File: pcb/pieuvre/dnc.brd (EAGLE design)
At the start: 97.2 x 88 mm, 143 parts, among them IC1 LM2596S, IC2 74ACT244SC, Q1 IRF9321PBF, Q10 FDN337N, Q11 FDN337N, Q12 BSS138, Q13 BSS138, Q14 FDN337N, Q2 BSS670, Q3 BSS138, Q4 BSS670, Q5 BSS138, Q6 BSS316, Q7 BSS138, Q8 BSS138, Q9 BSS670, U1 MAX202CDWR, U2 74HCT595D, U3 TC7SU04F, U4 AL8805WS, U5 AL8805WS, U6 TC7SU04F, X1 USB

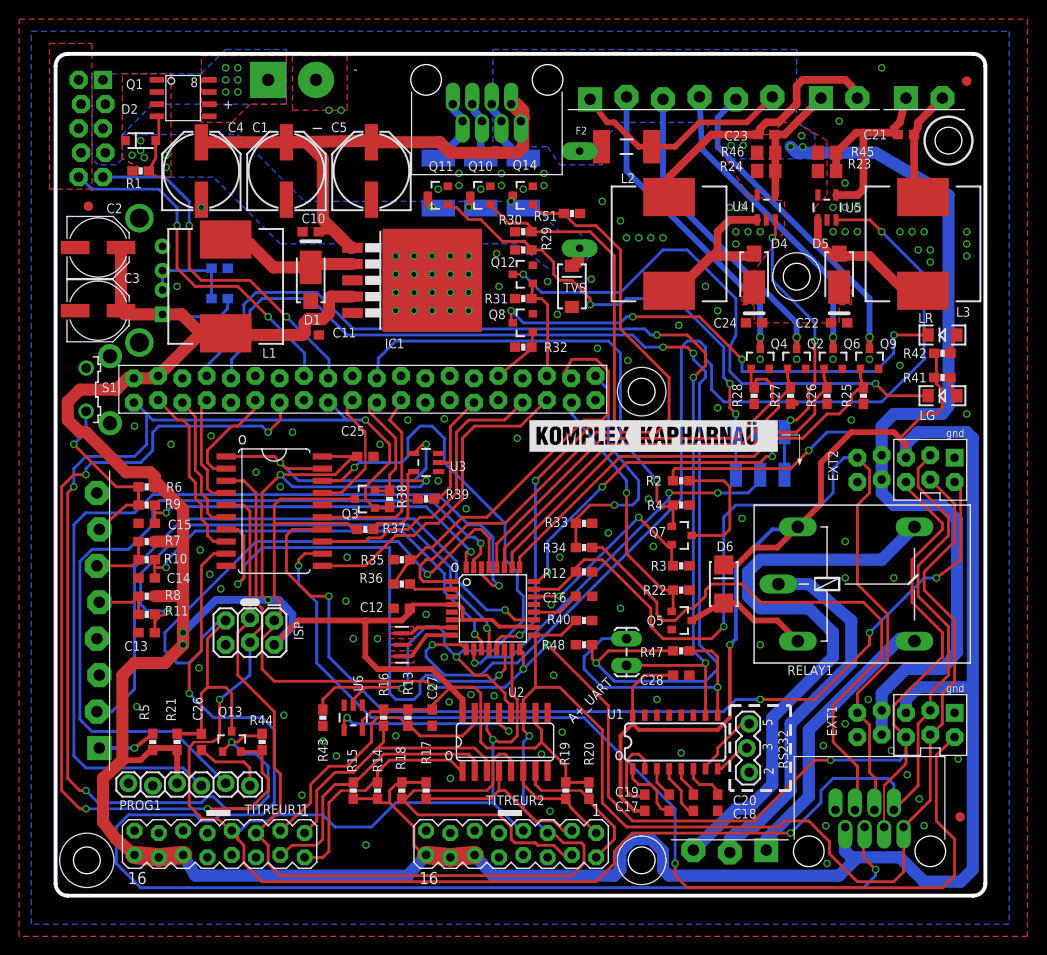
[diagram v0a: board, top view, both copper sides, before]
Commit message: major changes : - carte pieuvre - carte relais - correctif v1 : usb + pin A7 ! - enclosure
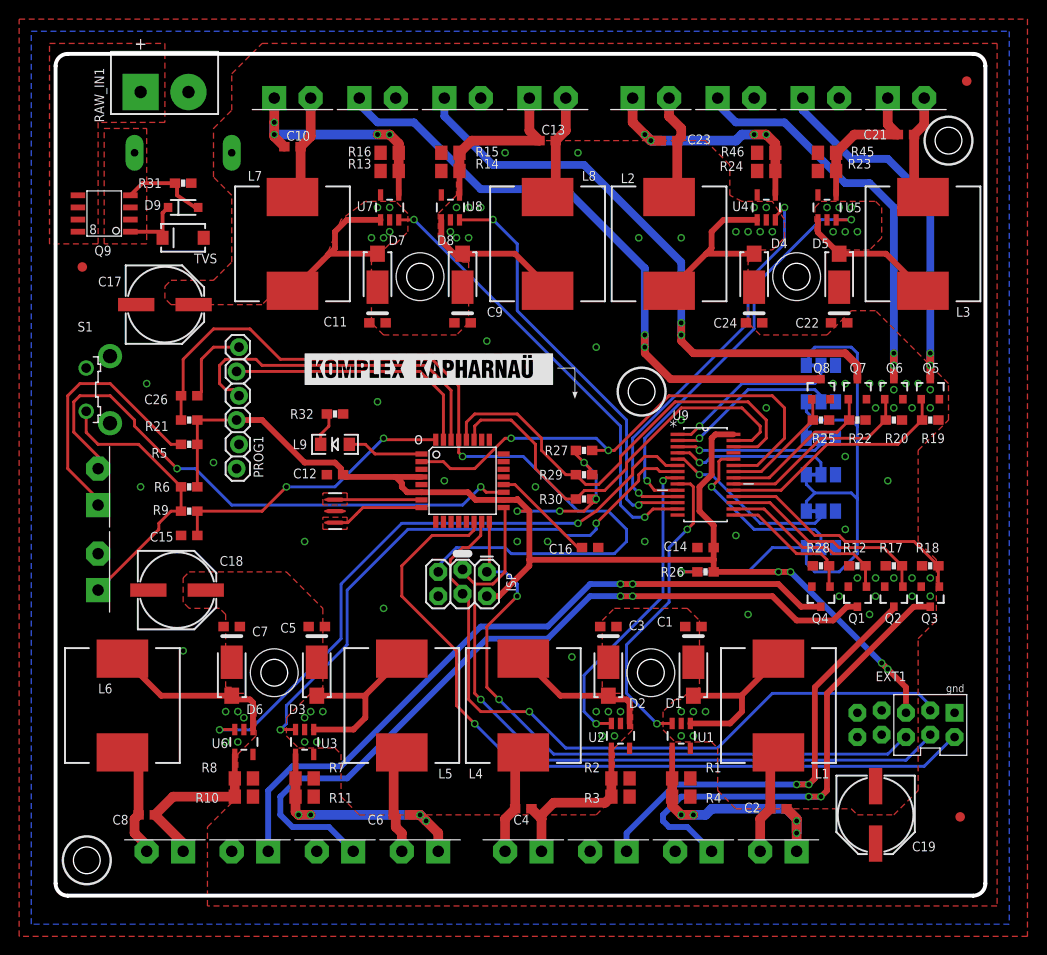
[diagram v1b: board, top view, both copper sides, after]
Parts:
- removed A+_UART: (no value), SparkFun:1X02_LOCK_LONGPADS
- removed C20, C25, C27, C28: 0.1uF, rcl:C0603
- removed EXT2: EXT, pierre_vv:EXTPINDNC
- removed F2, F3, F4, F5: PTC1812, pierre_vv:PTC_1812
- removed GYRO-LED: PLUG-6, pierre_vv:PLUG_06
- removed IC1: LM2596S, national-semiconductor:TO263-5
- removed IC2: 74ACT244SC, 74xx-us:SO20W
- removed INPUT: PLUG-8, pierre_vv:PLUG_08
- removed JP1: CHARGEUR, pierre_vv:2X5_LOCK
- removed LG, LR: (no value), SparkFun-LED:LED-1206
- removed Q10, Q11, Q14: FDN337N, SparkFun-DiscreteSemi:SOT23-3
- removed Q12, Q13: BSS138, SparkFun-DiscreteSemi:SOT23-3
- removed R33, R35, R48: 20K, SparkFun-Passives:0603-RES
- removed R34, R36, R37, R38, R39, R40, R43, R44, R47: 10K, SparkFun-Passives:0603-RES
- removed R41, R42: 1K, SparkFun-Passives:0603-RES
- removed R49: 22K, SparkFun-Passives:0603-RES
- removed R50: 33K, SparkFun-Passives:0603-RES
- removed R51: 100K, SparkFun-Passives:0603-RES
- removed RAW_IN: DNC_IN2PWR, pierre_vv:DNC_IN2_PWR
- removed RELAY: PLUG-3, pierre_vv:PLUG_03
- removed RELAY1: G5L, relay:G5LE
- removed RGB-LED: RJ45-RGBLED, con-amphenol-rj45-ld:RJ45-TRAFO
- removed RS232: (no value), SparkFun-Connectors:1X03_LOCK
- removed TITREUR1, TITREUR2: DNC_TITREUR, pierre_vv:DNC_TITREUR
- removed U$8: RJ45-EXTDNC, con-amphenol-rj45-ld:RJ45-TRAFO
- removed X1: USB, pierre_vv:USB_F_SATISTRONIC
- added C6, C8: 1uF, rcl:C0603
- added C7, C9: 0.1uF, rcl:C0603
- added D3, D7, D8: 40v5A, pierre_vv:DO-221
- added D9: 10V, SparkFun-DiscreteSemi:SOD-123
- added FAN1, FAN2, FAN3, FAN4, FAN5, FAN6, FAN7, FAN8, LED10W3, LED10W4, LED10W5, LED10W6, LED10W7, LED10W8, POT, SWITCH: PLUG-2, pierre_vv:PLUG_02
- added L4, L5, L6, L7, L8: 100nH2.4A, SparkFun:CDRH125
- added L9: LG, SparkFun-LED:LED-1206
- added RAW_IN1: DNC_IN2PWR, pierre_vv:DNC_IN2_PWR
- added SJ3, SJ4, SJ5, SJ6: JUMPER-PAD-3-2OF3_NC_BY_TRACE_LARGE, SparkFun-Passives:PAD-JUMPER-3-2OF3_NC_BY_TRACE_YES_SILK_LARGE
- added U$3, U$5: RADIATEUR, pierre_vv:RADIATEUR_577102B00000G
- added U7, U8: AL8805WS, SparkFun-PowerIC:SOT23-5
- added U9: PCA9685PW, pierre_vv:SOP65P640X110-28N
- C1, C5: value 220uF -> 0.1uF; device SparkFun:PANASONIC_E -> rcl:C0603
- C10: value 0.1uF -> 1uF
- C14: value 1uF -> 0.1uF
- C17, C18, C19: value 0.1uF -> 220uF; device rcl:C0603 -> SparkFun:PANASONIC_E
- C2: value 100u -> 1uF; device rcl:PANASONIC_D -> rcl:C0603
- C3: value 100u -> 0.1uF; device rcl:PANASONIC_D -> rcl:C0603
- C4: value 220uF -> 1uF; device SparkFun:PANASONIC_E -> rcl:C0603
- D2: value 10V -> 40v5A; device SparkFun-DiscreteSemi:SOD-123 -> pierre_vv:DO-221
- D6: value (none) -> 40v5A; device SparkFun-DiscreteSemi:SMA-DIODE_ALT -> pierre_vv:DO-221
- L1: value 68nH3A -> 100nH2.4A
- Q1: value IRF9321PBF -> BSS316; device pierre_vv:SO-8 -> SparkFun-DiscreteSemi:SOT23-3
- Q2, Q4: value BSS670 -> BSS316
- Q3, Q5, Q7, Q8: value BSS138 -> BSS316
- Q9: value BSS670 -> IRF9321PBF; device SparkFun-DiscreteSemi:SOT23-3 -> pierre_vv:SO-8
- R1, R13, R14: value 100K -> 0.110; device SparkFun-Passives:0603-RES -> rcl:R0805
- R10, R11: value 33K -> OPT; device SparkFun-Passives:0603-RES -> rcl:R0805
- R12: value 5.1K -> 100K
- R15, R16, R4: value 100K -> OPT; device SparkFun-Passives:0603-RES -> rcl:R0805
- R2: value 100k1% -> 0.110; device SparkFun-Passives:0603-RES -> rcl:R0805
- R26, R32: value 100K -> 1K
- R27, R29, R30: value 100K -> 10K
- R3: value 10k1% -> OPT; device SparkFun-Passives:0603-RES -> rcl:R0805
- R7, R8: value 56K -> 0.110; device SparkFun-Passives:0603-RES -> rcl:R0805
- SJ1, SJ2: value JUMPER-PAD-3-NO -> JUMPER-PAD-3-2OF3_NC_BY_TRACE_LARGE; device SparkFun-Passives:PAD-JUMPER-3-NO_YES_SILK_FULL_BOX_WIDE_SPACING -> SparkFun-Passives:PAD-JUMPER-3-2OF3_NC_BY_TRACE_YES_SILK_LARGE
- U$4: value RASPIA+ -> RADIATEUR; device pierre_vv:RASPIA+ -> pierre_vv:RADIATEUR_577102B00000G
- U1: value MAX202CDWR -> AL8805WS; device SparkFun-DigitalIC:SO016 -> SparkFun-PowerIC:SOT23-5
- U2: value 74HCT595D -> AL8805WS; device IC:SO16 -> SparkFun-PowerIC:SOT23-5
- U3, U6: value TC7SU04F -> AL8805WS; device SparkFun-DigitalIC:SOT23-5 -> SparkFun-PowerIC:SOT23-5
- moved LED10W1 111.8 mm to (11.4, 0.64), turned to 180 degrees
- moved C2 92.2 mm to (75.6, 5.08), turned to 180 degrees
- moved LED10W2 90.1 mm to (38.1, 0.64), turned to 180 degrees
- moved Q1 87.6 mm to (83.8, 27.3), turned to 180 degrees
- moved R1 85.0 mm to (65.4, 8.26), turned to 0 degrees
- moved Q9 81.4 mm to (5.08, 67.3), turned to 180 degrees
- moved C4 74.7 mm to (48.9, 5.08), turned to 180 degrees
- moved D2 74.3 mm to (57.8, 19.1), turned to 90 degrees
- moved C17 74.1 mm to (11.4, 57.8), turned to 0 degrees
- moved L1 72.5 mm to (75.6, 15.9)
- moved U$4 69.8 mm to (38.1, 60.7), flipped to the bottom
- moved R15 67.4 mm to (41.3, 73.7), turned to 180 degrees
- moved C13 66.3 mm to (51.4, 74.9), turned to 0 degrees
- moved R14 65.2 mm to (41.3, 71.8), turned to 180 degrees
- moved C1 63.9 mm to (66.7, 24.1), turned to 0 degrees
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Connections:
- removed net +3V3: Q13.1, Q3.1, R38.2, R44.2, U$4.1, U$4.17
- removed net /REG_RCK_5V=ACTIVE_CS: U2.13, U6.4
- removed net ALL_CS_ENABLE_ACTIVE_LOW_5V: IC2.1, IC2.19, U3.4
- removed net ANALOG_RAW: AT328.22, Q7.2, R3.2
- removed net ATMEGA_CS: IC2.13, U$4.33
- removed net ATMEGA_CS_5V: AT328.14, IC2.7
- removed net CHARGING: JP1.2, U$4.16
- removed net CS_TRIGGER_ACTIVE_HIGH: R39.2, U$4.29, U3.2
- removed net DIGITAL_LED2_OR_FLEX3: AT328.24, SJ1.2
- removed net EXT1_CS: IC2.8, U$4.3
- removed net EXT2_CS: IC2.6, U$4.5
- removed net EXT2_CS_5V: EXT2./CS, IC2.14
- removed net EXT3_CS: IC2.4, U$4.7
- removed net EXT3_CS_5V: IC2.16
- removed net GYRO_1: AT328.28, Q4.1, R28.2
- removed net GYRO_2: AT328.27, Q2.1, R27.2
- removed net GYRO_3: AT328.26, Q6.1, R26.2
- removed net GYRO_4: AT328.25, Q9.1, R25.2
- removed net INT_ATMEGA: R35.2, R36.1, U$4.38
- removed net INT_ATMEGA_5V: AT328.2, R36.2
- removed net INT_TELECO: R33.2, R34.1, U$4.40
- removed net INT_TELECO_5V: R34.2, U$8.4
- removed net LEDR: LR.C, Q8.3
- removed net LED_G: Q12.1, R31.2, U$4.36
- removed net LED_R: Q8.1, R32.2, U$4.32
- removed net LG: LG.C, Q12.3
- removed net MISO: Q3.2, R38.1, U$4.21
- removed net MOSI: IC2.17, U$4.19
- removed net N$1: D1.C, IC1.2, L1.1
- removed net N$19: F3.1, Q10.3
- removed net N$20: INPUT.6, R10.1, R7.1
- removed net N$21: LR.A, R42.1
- removed net N$23: INPUT.5, R11.1, R8.1
- removed net N$24: C19.2, U1.2
- removed net N$26: R49.2, R50.2, X1.DM, X1.DP
- removed net N$29: F5.2, RGB-LED.3, RGB-LED.4
- removed net N$50: C18.2, U1.5
- removed net N$51: C18.1, U1.4
- removed net N$52: C17.2, U1.3
- removed net N$53: C17.1, U1.1
- removed net PRXD_PIN2_RS232: RS232.1, U1.7
- removed net PTXD_PIN3_RS232: RS232.2, U1.8
- removed net PUSH2: AT328.11, C14.1, R10.2
- removed net PUSH3: AT328.12, C13.1, R11.2
- removed net PWM_FLEX_1: AT328.1, Q14.1, R51.2
- removed net PWM_FLEX_2: AT328.13, Q10.1, R30.2
- removed net PWM_FLEX_3: Q11.1, R29.2, SJ1.3, SJ2.3
- removed net PWM_LED2_OR_FLEX3: AT328.10, SJ2.2
- removed net RAW_POL_PROTECTED: D2.C, F1.P$1MOV, Q1.1, Q1.2, Q1.3, TVS.C
- removed net RAW_UNPROTECTED: JP1.3, JP1.5, JP1.7, JP1.9, Q1.5, Q1.6, Q1.7, Q1.8, RAW_IN.1
- removed net READ_BATTERY: Q7.1, R4.2, U$4.22
- removed net REG_RCK: IC2.2, U$4.11
- removed net REG_RCK_5V: IC2.18, R43.2, U2.12, U6.2
- removed net RELAY1: Q5.1, R22.2, U$4.37
- removed net RELAY_CHARGE_BOARD: JP1.1, U$4.18
- removed net RESET: Q13.2, R44.1, U$4.13
- removed net RST1: R16.1, TITREUR1.1, U2.3
- removed net RST2: R14.1, TITREUR1.2, U2.1
- removed net RST3: R13.1, TITREUR1.3, U2.15
- removed net RST4: R15.1, TITREUR1.4, U2.2
- removed net RST5: R19.1, TITREUR2.1, U2.6
- removed net RST6: R20.1, TITREUR2.2, U2.7
- removed net RST7: R17.1, TITREUR2.3, U2.4
- removed net RST8: R18.1, TITREUR2.4, U2.5
- removed net RXA+: R47.1, R48.2, U$4.10
- removed net RXA+_5V: A+_UART.2, R47.2, U1.9
- removed net SCK: IC2.15, U$4.23
- removed net TELECO_CS: IC2.11, U$4.35
- removed net TELECO_CS_5V: IC2.9, U$8.3
- removed net TXA+_5V: A+_UART.1, U$4.8, U1.10
- new net A0: SJ1.2, U9.1
- new net A1: SJ2.2, U9.2
- new net A2: SJ3.2, U9.3
- new net A3: SJ4.2, U9.4
- new net A4: SJ5.2, U9.5
- new net A5: SJ6.2, U9.24
- new net LED: AT328.1, L9.A
- new net LED+3: C4.1, LED10W3.1, R2.1, R3.1, U2.4
- new net LED+4: C2.1, LED10W4.1, R1.1, R4.1, U1.4
- new net LED+5: C21.1, LED10W5.1, R23.1, R45.1, U5.4
- new net LED+6: C23.1, LED10W6.1, R24.1, R46.1, U4.4
- new net LED+7: C13.1, LED10W7.1, R14.1, R15.1, U8.4
- new net LED+8: C10.1, LED10W8.1, R13.1, R16.1, U7.4
- new net LED-3: C4.2, L4.2, LED10W3.2
- new net LED-4: C2.2, L1.2, LED10W4.2
- new net LED-5: C21.2, L3.2, LED10W5.2
- new net LED-6: C23.2, L2.2, LED10W6.2
- new net LED-7: C13.2, L8.2, LED10W7.2
- new net LED-8: C10.2, L7.2, LED10W8.2
- new net OE: AT328.2, R27.1, U9.23
- new net PWM_FAN1: Q4.1, R28.2, U9.15
- new net PWM_FAN2: Q1.1, R12.2, U9.16
- new net PWM_FAN3: Q2.1, R17.2, U9.17
- new net PWM_FAN4: Q3.1, R18.2, U9.18
- new net PWM_FAN5: Q5.1, R19.2, U9.19
- new net PWM_FAN6: Q6.1, R20.2, U9.20
- new net PWM_FAN7: Q7.1, R22.2, U9.21
- new net PWM_FAN8: Q8.1, R25.2, U9.22
- new net PWM_LED_3: U2.3, U9.8
- new net PWM_LED_4: U1.3, U9.9
- new net PWM_LED_5: U5.3, U9.10
- new net PWM_LED_6: U4.3, U9.11
- new net PWM_LED_7: U8.3, U9.12
- new net PWM_LED_8: U7.3, U9.13
- new net RAW_POL_PROTECTED1: D9.C, F1.P$1MOV, Q9.1, Q9.2, Q9.3, TVS.C
- new net RAW_UNPROTECTED1: Q9.5, Q9.6, Q9.7, Q9.8, RAW_IN1.1
- new net SCL: AT328.28, R29.1, U9.26
- new net SDA: AT328.27, R30.1, U9.27
- net +5V: now also C14.1, R26.2, R27.2, R29.2, R30.2, U9.28; no longer C11.1, C19.1, C2.+, C25.1, C27.1, C28.1, C3.+, D6.C, EXT2.5V, IC1.4, IC2.20, L1.2, R13.2, R14.2, R15.2, R16.2, R17.2, R18.2, R19.2, R20.2, R37.2, R41.2, R42.2, R50.1, R7.2, R8.2, RELAY1.2, TITREUR1.12, TITREUR1.14, TITREUR1.16, TITREUR2.12, TITREUR2.14, TITREUR2.16, U$4.2, U$4.4, U$8.1, U1.16, U2.10, U2.16, U3.5, U6.5, X1.+
- net CODE: no longer AT328.23, EXT2.RETOURANALOG, R12.1, U$8.6
- net EXT1_CS_5V: now also AT328.14; no longer IC2.12
- net FLOAT1: now also POT.2; no longer INPUT.2
- net GND: now also C1.2, C17.-, C18.-, C19.-, C3.2, C5.2, C7.2, C9.2, Q1.2, Q3.2, Q7.2, R12.1, R17.1, R18.1, R19.1, R20.1, R31.2, R32.2, RAW_IN1.2, SJ1.1, SJ2.1, SJ3.1, SJ4.1, SJ5.1, SJ6.1, SWITCH.2, U1.2, U2.2, U3.2, U6.2, U7.2, U8.2, U9.14, U9.25; no longer C1.-, C10.2, C13.2, C2.-, C20.2, C25.2, C27.2, C28.2, C3.-, C4.-, C5.-, D1.A, EXT2.1_GND, EXT2.GND2, IC1.3, IC1.5, IC1.THERMAL, IC2.10, INPUT.4, INPUT.8, JP1.10, JP1.4, JP1.6, JP1.8, Q10.2, Q11.2, Q12.2, Q14.2, Q9.2, R1.2, R12.2, R26.1, R27.1, R29.1, R3.1, R30.1, R31.1, R32.1, R33.1, R35.1, R39.1, R4.1, R40.1, R43.1, R48.1, R49.1, R51.1, RAW_IN.2, RS232.3, TITREUR1.11, TITREUR1.13, TITREUR1.15, TITREUR1.8, TITREUR2.11, TITREUR2.13, TITREUR2.15, TITREUR2.8, U$4.14, U$4.20, U$4.25, U$4.30, U$4.34, U$4.39, U$4.6, U$4.9, U$8.2, U1.15, U2.8, U3.3, U6.3, X1.-, X1.S1, X1.S2
- net LED+1: now also C6.1, R11.1, R7.1, U3.4; no longer C23.1, R24.1, R46.1, U4.4
- net LED+2: now also C8.1, R10.1, R8.1, U6.4; no longer C21.1, R23.1, R45.1, U5.4
- net LED-1: now also C6.2, L5.2; no longer C23.2, L2.2
- net LED-2: now also C8.2, L6.2; no longer C21.2, L3.2
- net MISO_5V: no longer EXT2.MISO, Q3.3, R37.1, U$8.5
- net MOSI_5V: no longer EXT2.MOSI, IC2.3, TITREUR1.7, TITREUR2.7, U$8.8, U2.14
- net N$10: now also D7.A, L7.1, U7.1; no longer GYRO-LED.2, Q4.3
- net N$11: now also D8.A, L8.1, U8.1; no longer GYRO-LED.3, Q2.3
- net N$12: now also FAN2.1, Q1.3; no longer GYRO-LED.4, Q6.3
- net N$13: now also FAN3.1, Q2.3; no longer GYRO-LED.5, Q9.3
- net N$14: now also FAN4.1, Q3.3; no longer F4.2, RGB-LED.7, RGB-LED.8
- net N$15: now also FAN5.1, Q5.3; no longer RELAY.3, RELAY1.O
- net N$16: now also FAN6.1, Q6.3; no longer D6.A, Q5.3, RELAY1.1
- net N$17: now also FAN7.1, Q7.3; no longer F4.1, Q11.3
- net N$18: now also FAN8.1, Q8.3; no longer LG.A, R41.1
- net N$22: now also SWITCH.1; no longer INPUT.7
- net N$25: now also POT.1; no longer INPUT.1
- net N$3: now also D1.A, L1.1, U1.1; no longer Q7.3, R2.1
- net N$30: now also R26.1, SJ1.3, SJ2.3, SJ3.3, SJ4.3, SJ5.3, SJ6.3; no longer F5.1, Q14.3
- net N$35: now also L9.C, R32.1; no longer C20.1, U1.6
- net N$4: now also FAN1.1, Q4.3; no longer RELAY.1, RELAY1.S
- net N$5: now also D2.A, L4.1, U2.1; no longer F2.2, GYRO-LED.1, GYRO-LED.6
- net N$8: now also D3.A, L5.1, U3.1; no longer RELAY.2, RELAY1.P
- net N$9: now also D6.A, L6.1, U6.1; no longer F3.2, RGB-LED.5, RGB-LED.6
- net PROTECT_GATE: now also D9.A, Q9.4, R31.1; no longer D2.A, Q1.4, R1.1
- net PWM_LED_1: now also U6.3, U9.6; no longer AT328.9, U5.3
- net PWM_LED_2: now also U3.3, U9.7; no longer SJ1.1, SJ2.1, U4.3
- net RAW_FUSED: now also C1.1, C11.1, C17.+, C18.+, C19.+, C3.1, C5.1, C7.1, C9.1, D1.C, D2.C, D3.C, D6.C, D7.C, D8.C, FAN1.2, FAN2.2, FAN3.2, FAN4.2, FAN5.2, FAN6.2, FAN7.2, FAN8.2, R1.2, R10.2, R11.2, R13.2, R14.2, R15.2, R16.2, R3.2, R4.2, R7.2, R8.2, U1.5, U2.5, U3.5, U6.5, U7.5, U8.5; no longer C1.+, C10.1, C4.+, C5.+, EXT1.RAW, EXT1.RAW2, EXT2.RAW, EXT2.RAW2, F2.1, IC1.1, RGB-LED.1, RGB-LED.2
- net RESET_5V: no longer Q13.3
- net SCK_5V: no longer EXT2.SCK, IC2.5, R40.2, TITREUR1.5, TITREUR2.5, U$8.7, U2.11
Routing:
- net +5V: track 579.0 -> 145.5 mm, vias 6 -> 8
- net RAW_FUSED: track 180.6 -> 0.00 mm, vias 6 -> 0
- net MOSI_5V: track 227.8 -> 74.8 mm, vias 3 -> 1
- net TELECO_CS_5V: track 143.6 -> 0.00 mm, vias 2 -> 0
- net SCK_5V: track 211.8 -> 75.7 mm
- net +3V3: track 123.3 -> 0.00 mm, vias 4 -> 0
- net RXA+: track 116.4 -> 0.00 mm, vias 3 -> 0
- net TXA+_5V: track 108.2 -> 0.00 mm, vias 3 -> 0
- net EXT2_CS_5V: track 103.6 -> 0.00 mm, vias 4 -> 0
- net MISO_5V: track 169.7 -> 68.6 mm, vias 4 -> 2
- net CODE: track 97.4 -> 0.00 mm, vias 1 -> 0
- net RESET: track 91.3 -> 0.00 mm, vias 4 -> 0
- net REG_RCK_5V: track 81.7 -> 0.00 mm, vias 3 -> 0
- net N$30: track 2.23 -> 70.4 mm
- net PWM_FLEX_1: track 68.1 -> 0.00 mm
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- added copper zone on layer 1, net RAW_POL_PROTECTED1
- added copper zone on layer 1, net RAW_UNPROTECTED1
- removed copper zone on layer 16, net RAW_FUSED
- removed copper zone on layer 1, net RAW_POL_PROTECTED
- removed copper zone on layer 16, net RAW_POL_PROTECTED
- removed copper zone on layer 1, net RAW_UNPROTECTED
- removed copper zone on layer 16, net RAW_UNPROTECTED
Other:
- board text removed: "+"
- board text removed: "-"
- board text removed: "2"
- board text removed: "3"
- board text removed: "5"
- board text removed: "5V IPOD"
- board text removed: "BRD+10mm"
- board text removed: "BRD+13,5mm"
- board text removed: "BRD+8mm"
- board text removed: "CARTE DNC V0.3"
- board text removed: "DIGITAL"
- board text removed: "FLEX B"
- board text removed: "LED 10W 2"
- board text removed: "PWM"
- board text removed: "Pierre H Olivier R"
- board text removed: "RPI+3mm"
- board text removed: "RPI+3mm diam15mm"
- board text removed: "RPI+6mm"
- board text removed: "RPI+7mm"
- board text removed: "RPI-2mm"
- board text removed: "fev 2015"
- board text removed: "titreur BRD+7mm"
